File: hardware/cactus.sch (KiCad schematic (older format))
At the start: 20 parts, among them SW1 SW_Push, U1 WeMos_Battery_Shield, U2 WeMos_D1_mini, U3 74HC595, U4 Si7021_breakout

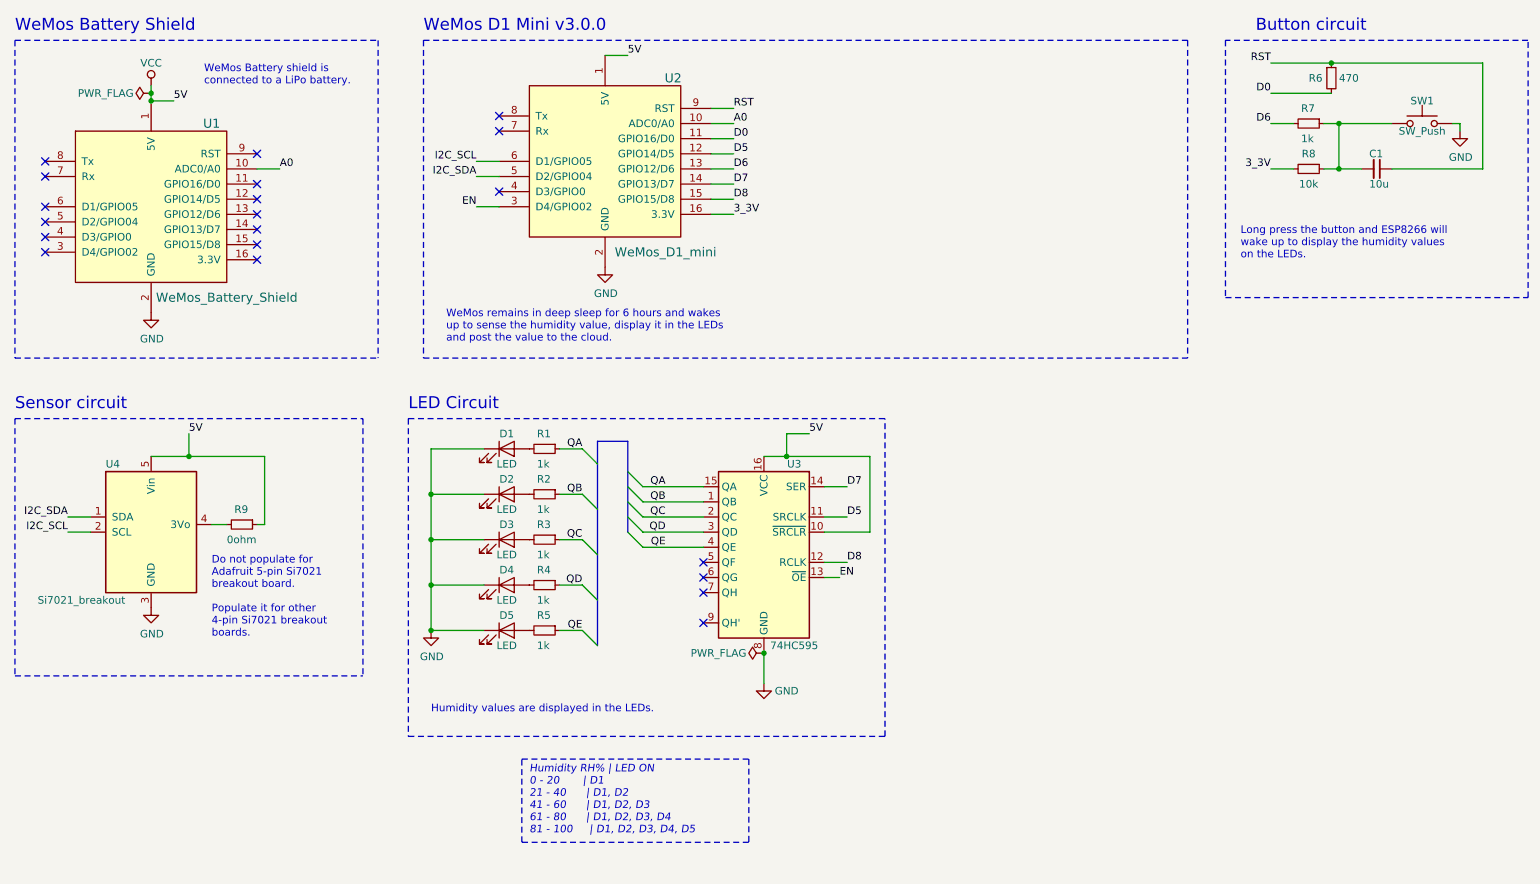
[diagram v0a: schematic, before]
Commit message: [si] Add battery version and 100k ohm instructions
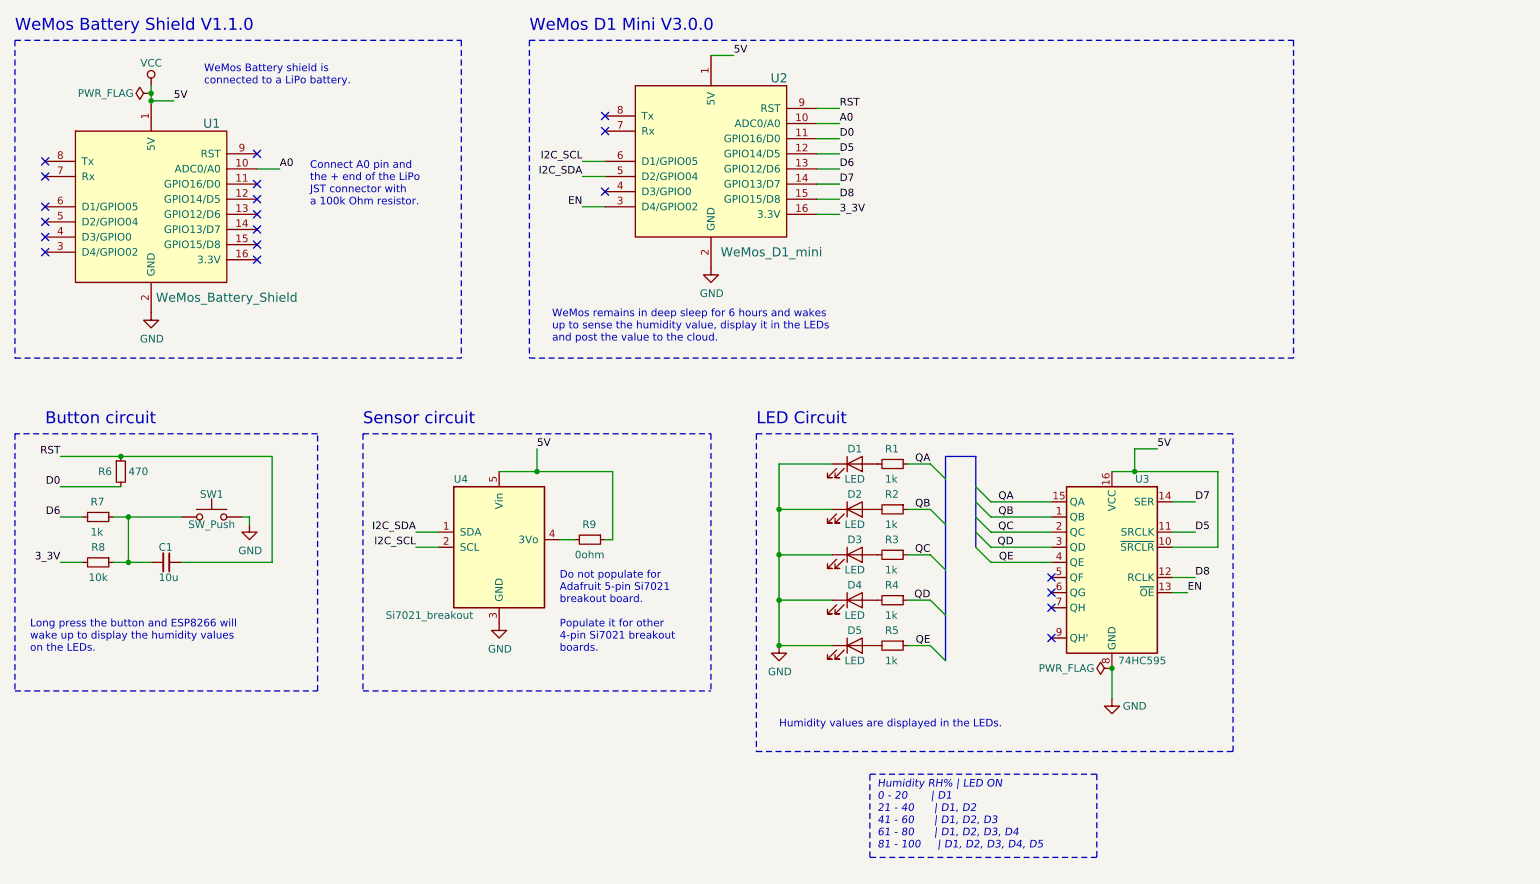
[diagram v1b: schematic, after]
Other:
- note added: "Connect A0 pin and \nthe + end of the LiPo \nJST connector with \na 100k Ohm resistor."
- note added: "WeMos Battery Shield V1.1.0"
- note added: "WeMos D1 Mini V3.0.0"
- note removed: "WeMos Battery Shield"
- note removed: "WeMos D1 Mini v3.0.0"
- moved on the sheet: C1, D1, D2, D3, D4, D5, R1, R2, R3, R4, R5, R6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

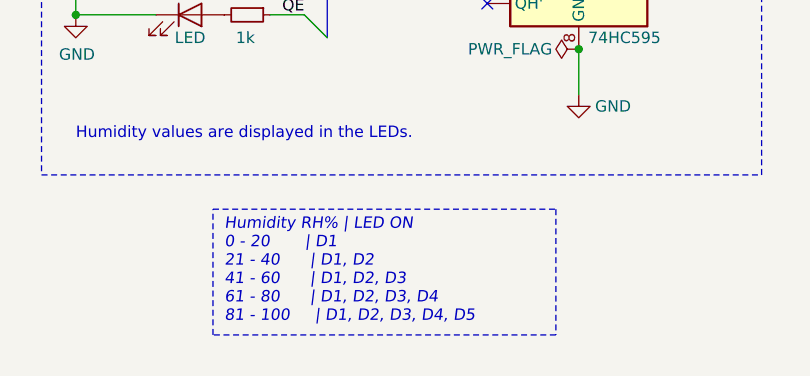
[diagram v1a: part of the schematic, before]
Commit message: [si] Amend bar display for humidity
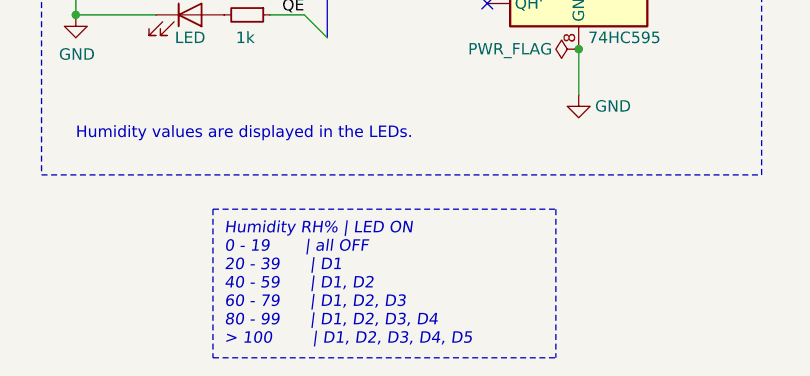
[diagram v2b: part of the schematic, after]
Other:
- note added: "Humidity RH% | LED ON\n0 - 19 | all OFF\n20 - 39 | D1\n40 - 59 | D1, D2\n60 - 79 | D1, D2, D3\n80 - 99 | D1, D2, D3, D4\n> 100 | D1, D2, D3, D4, D5"
- note removed: "Humidity RH% | LED ON\n0 - 20 | D1\n21 - 40 | D1, D2\n41 - 60 | D1, D2, D3\n61 - 80 | D1, D2, D3, D4\n81 - 100 | D1, D2, D3, D4, D5"
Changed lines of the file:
@@
 Text Notes 4450 2900 0    50   ~ 0
 WeMos remains in deep sleep for 6 hours and wakes \nup to sense the humidity value, display it in the LEDs \nand post the value to the cloud.
-Text Notes 6600 6250 0    50   Italic 0
-Humidity RH% | LED ON\n0 - 20       | D1\n21 - 40      | D1, D2\n41 - 60      | D1, D2, D3\n61 - 80      | D1, D2, D3, D4\n81 - 100     | D1, D2, D3, D4, D5
+Text Notes 6600 6350 0    50   Italic 0
+Humidity RH% | LED ON\n0 - 19       | all OFF\n20 - 39      | D1\n40 - 59      | D1, D2\n60 - 79      | D1, D2, D3\n80 - 99      | D1, D2, D3, D4\n> 100        | D1, D2, D3, D4, D5
 Wire Notes Line
 	6550 5750 8050 5750
-Wire Notes Line
-	8050 6300 6550 6300
-Wire Notes Line
-	6550 6300 6550 5750
-Wire Notes Line
-	8050 5750 8050 6300
 Text Notes 5950 5450 0    50   ~ 0
 Humidity values are displayed in the LEDs.
@@
 Data
 89 50 4E 47 0D 0A 1A 0A 00 00 00 0D 49 48 44 52 00 00 03 60 00 00 03 61 08 02 00 00 00 0E AC 4F
-56 00 00 00 03 73 42 49 54 08 08 08 DB E1 4F E0 00 00 00 09 70 48 59 73 00 00 0B 12 00 00 0B 12
-01 D2 DD 7E FC 00 00 20 00 49 44 41 54 78 9C EC BD EB AF EC B8 B2 1F 56 0F 52 DD 6B ED C7 CC 9C
+56 00 00 00 03 73 42 49 54 08 08 08 DB E1 4F E0 00 00 00 09 70 48 59 73 00 00 0A F0 00 00 0A F0
+01 42 AC 34 98 00 00 20 00 49 44 41 54 78 9C EC BD EB AF EC B8 B2 1F 56 0F 52 DD 6B ED C7 CC 9C
 E3 73 6E E0 9B 5C 03 86 F3 E1 E6 43 80 FC FF FF 40 F2 C5 30 90 38 31 90 D8 B8 B1 CF B5 73 66 CE
 BC F6 63 75 B7 C8 AA CA 07 AA B5 D4 7A B5 D4 92 BA D5 6B F7 6F 80 41 6F 2D 8A 2C 92 C5 62 BD 48
@@
 Wire Notes Line
 	900  3000 3850 3000
+Wire Notes Line
+	6550 6400 8050 6400
+Wire Notes Line
+	6550 5750 6550 6400
+Wire Notes Line
+	8050 5750 8050 6400
 Wire Bus Line
 	7250 3650 7250 4250

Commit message: [docs] Transfer library files as git submodule
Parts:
- removed U1: WeMos_Battery_Shield, WeMos:Battery_shield, symbol cactus-rescue:WeMos_Battery_Shield-wemos_mini
- removed U4: Si7021_breakout, Connector_PinHeader_2.54mm:PinHeader_1x05_P2.54mm_Vertical, symbol cactus-rescue:Si7021_breakout-Si7021_breakout_board
- added U1: WeMos_Battery_Shield, symbol WeMos_D1_Mini_board:WeMos_Battery_Shield
- added U4: Si7021_breakout, symbol Adafruit_Si7021_breakout:Si7021_breakout
- U2: symbol cactus-rescue:WeMos_D1_mini-wemos_mini -> WeMos_D1_Mini_board:WeMos_D1_mini
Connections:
- wire segments 68 -> 69
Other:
- moved on the sheet: R9
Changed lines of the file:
@@
 L power:GND #PWR01
 U 1 1 5C89C91B
-P 4100 4750
-F 0 "#PWR01" H 4100 4500 50  0001 C CNN
-F 1 "GND" H 4105 4577 50  0000 C CNN
-F 2 "" H 4100 4750 50  0001 C CNN
-F 3 "" H 4100 4750 50  0001 C CNN
-	1    4100 4750
+P 4050 4550
+F 0 "#PWR01" H 4050 4300 50  0001 C CNN
+F 1 "GND" H 4055 4377 50  0000 C CNN
+F 2 "" H 4050 4550 50  0001 C CNN
+F 3 "" H 4050 4550 50  0001 C CNN
+	1    4050 4550
 	1    0    0    -1
 $EndComp
@@
 NoConn ~ 1100 2300
 $Comp
-L cactus-rescue:WeMos_D1_mini-wemos_mini U2
+L WeMos_D1_Mini_board:WeMos_D1_mini U2
 U 1 1 5C9440E1
 P 5500 1700
@@
 Wire Wire Line
 	1800 1300 1950 1300
-Connection ~ 1800 1300
-$Comp
-L cactus-rescue:WeMos_Battery_Shield-wemos_mini U1
-U 1 1 5C954F32
-P 1800 2000
-F 0 "U1" H 2200 2550 60  0000 C CNN
-F 1 "WeMos_Battery_Shield" H 2300 1400 60  0000 C CNN
-F 2 "WeMos:Battery_shield" H 2200 1300 60  0001 C CNN
-F 3 "https://wiki.wemos.cc/products:d1_mini_shields:battery_shield" H 1800 2794 60  0001 C CNN
-	1    1800 2000
-	1    0    0    -1
-$EndComp
 Wire Notes Line
 	900  900  900  3000
@@
 Wire Notes Line
 	4300 900  4300 3000
-$Comp
-L cactus-rescue:Si7021_breakout-Si7021_breakout_board U4
-U 1 1 5C97D9C5
-P 4100 4250
-F 0 "U4" H 3800 4700 50  0000 L CNN
-F 1 "Si7021_breakout" H 3350 3800 50  0000 L CNN
-F 2 "Connector_PinHeader_2.54mm:PinHeader_1x05_P2.54mm_Vertical" H 4100 3650 50  0001 C CNN
-F 3 "https://learn.adafruit.com/adafruit-si7021-temperature-plus-humidity-sensor/downloads" H 4100 4050 50  0001 C CNN
-	1    4100 4250
-	1    0    0    -1
-$EndComp
 Wire Wire Line
 	3700 4150 3550 4150
@@
 L Device:R_Small R9
 U 1 1 5C9E0F92
-P 4700 4200
-F 0 "R9" V 4600 4150 50  0000 L CNN
-F 1 "0ohm" V 4800 4100 50  0000 L CNN
-F 2 "Resistor_SMD:R_0805_2012Metric_Pad1.15x1.40mm_HandSolder" H 4700 4200 50  0001 C CNN
-F 3 "~" H 4700 4200 50  0001 C CNN
-	1    4700 4200
+P 4700 4150
+F 0 "R9" V 4600 4100 50  0000 L CNN
+F 1 "0ohm" V 4800 4050 50  0000 L CNN
+F 2 "Resistor_SMD:R_0805_2012Metric_Pad1.15x1.40mm_HandSolder" H 4700 4150 50  0001 C CNN
+F 3 "~" H 4700 4150 50  0001 C CNN
+	1    4700 4150
 	0    1    1    0
 $EndComp
 Wire Wire Line
-	4500 4200 4600 4200
-Wire Wire Line
 	4350 3750 4350 3600
-Wire Wire Line
-	4100 3750 4350 3750
 Connection ~ 4350 3750
 Text Notes 4500 4950 0    50   ~ 0
 Do not populate for \nAdafruit 5-pin Si7021 \nbreakout board. \n\nPopulate it for other \n4-pin Si7021 breakout \nboards.
 Wire Wire Line
-	4850 3750 4850 4200
-Wire Wire Line
-	4850 4200 4800 4200
-Wire Wire Line
 	4350 3750 4850 3750
 Wire Notes Line
@@
 Wire Notes Line
 	8050 5750 8050 6400
+$Comp
+L Adafruit_Si7021_breakout:Si7021_breakout U4
+U 1 1 5CE67193
+P 4050 4200
+F 0 "U4" H 3750 4450 50  0000 L CNN
+F 1 "Si7021_breakout" H 3300 3850 50  0000 L CNN
+F 2 "" H 4050 3600 50  0000 C CNN
+F 3 "https://learn.adafruit.com/adafruit-si7021-temperature-plus-humidity-sensor/overview" H 4050 4000 50  0001 C CNN
+	1    4050 4200
+	1    0    0    -1
+$EndComp
+Wire Wire Line
+	4050 3750 4050 3900
+Wire Wire Line
+	4050 3750 4350 3750
+Wire Wire Line
+	4400 4150 4600 4150
+Wire Wire Line
+	4850 3750 4850 4150
+Wire Wire Line
+	4850 4150 4800 4150
+$Comp
+L WeMos_D1_Mini_board:WeMos_Battery_Shield U1
+U 1 1 5CE67330
+P 1800 2000
+F 0 "U1" H 2250 2550 60  0000 C CNN
+F 1 "WeMos_Battery_Shield" H 2300 1400 60  0000 C CNN
+F 2 "" H 2200 1300 60  0000 C CNN
+F 3 "http://www.wemos.cc/Products/d1_mini.html" H 1800 2797 60  0001 C CNN
+	1    1800 2000
+	1    0    0    -1
+$EndComp
+Connection ~ 1800 1300
 Wire Bus Line
 	7250 3650 7250 4250

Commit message: [schematic] Add a note on a bodge to control sensor Vin digitally
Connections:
- net labels added: EN_SENSOR
- no-connect marks 20 -> 19
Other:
- note added: "Do not populate R9 for \nAdafruit 5-pin Si7021 \nbreakout board. \n\nPopulate it for other \n4-pin Si7021 breakout \nboards."
- note added: "EN_SENSOR\nis a bodge of \nVersion 1.0 PCB \nlayout so that\nsensor can be \nturned on/off\ndigitally. It is \nconnected to \n5V directly on\nthe PCB."
- note removed: "Do not populate for \nAdafruit 5-pin Si7021 \nbreakout board. \n\nPopulate it for other \n4-pin Si7021 breakout \nboards."
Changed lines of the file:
@@
 EESchema Schematic File Version 4
-LIBS:cactus-cache
 EELAYER 29 0
 EELAYER END
@@
 NoConn ~ 4800 1400
 NoConn ~ 4800 1500
-NoConn ~ 4800 1900
 Wire Bus Line
 	7050 3650 7250 3650
@@
 Wire Wire Line
 	3700 4250 3550 4250
-Text Label 4350 3600 0    50   ~ 0
-5V
 Wire Wire Line
 	8550 4550 8650 4550
@@
 Wire Wire Line
 	4350 3750 4350 3600
-Connection ~ 4350 3750
-Text Notes 4500 4950 0    50   ~ 0
-Do not populate for \nAdafruit 5-pin Si7021 \nbreakout board. \n\nPopulate it for other \n4-pin Si7021 breakout \nboards.
+Text Notes 4350 4900 0    50   ~ 0
+Do not populate R9 for \nAdafruit 5-pin Si7021 \nbreakout board. \n\nPopulate it for other \n4-pin Si7021 breakout \nboards.
 Wire Wire Line
 	4350 3750 4850 3750
@@
 Wire Notes Line
 	3200 5200 5500 5200
-Wire Notes Line
-	3200 3500 5500 3500
 Text Label 8450 3600 0    50   ~ 0
 5V
@@
 $EndComp
 Wire Wire Line
-	4050 3750 4050 3900
-Wire Wire Line
-	4050 3750 4350 3750
-Wire Wire Line
 	4400 4150 4600 4150
 Wire Wire Line
@@
 $EndComp
 Connection ~ 1800 1300
-Wire Bus Line
-	7250 3650 7250 4250
+Wire Wire Line
+	4050 3750 4050 3900
+Connection ~ 4350 3750
+Wire Wire Line
+	4050 3750 4350 3750
+Text Label 4800 1900 2    50   ~ 0
+EN_SENSOR
+Text Label 4350 3600 0    50   ~ 0
+EN_SENSOR
+Text Notes 4950 4200 0    39   Italic 0
+EN_SENSOR\nis a bodge of \nVersion 1.0 PCB \nlayout so that\nsensor can be \nturned on/off\ndigitally. It is \nconnected to \n5V directly on\nthe PCB.
+Wire Notes Line
+	4900 4250 5500 4250
+Wire Notes Line
+	3200 3500 5500 3500
 Wire Bus Line
 	7050 3650 7050 5000
+Wire Bus Line
+	7250 3650 7250 4250
+Wire Notes Line
+	4900 3500 4900 4250
 $EndSCHEMATC

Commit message: chore: update KiCad 5.1.5
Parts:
- U4: symbol Adafruit_Si7021_breakout:Si7021_breakout -> Si7021_Breakout_board:Si7021_breakout
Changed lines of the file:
@@
 EESchema Schematic File Version 4
-EELAYER 29 0
+EELAYER 30 0
 EELAYER END
 $Descr A4 11693 8268
@@
 	8050 5750 8050 6400
 $Comp
-L Adafruit_Si7021_breakout:Si7021_breakout U4
+L Si7021_Breakout_board:Si7021_breakout U4
 U 1 1 5CE67193
 P 4050 4200
@@
 Wire Notes Line
 	3200 3500 5500 3500
+Wire Notes Line
+	4900 3500 4900 4250
 Wire Bus Line
 	7050 3650 7050 5000
 Wire Bus Line
 	7250 3650 7250 4250
-Wire Notes Line
-	4900 3500 4900 4250
 $EndSCHEMATC
